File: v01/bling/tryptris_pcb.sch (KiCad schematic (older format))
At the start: 133 parts, among them J1 USB_C_Receptacle_USB2.0, J2 I2C-L, J3 I2C-R, J4 AVR-ISP-6, SW1 Reset, U1 ATmega32U4-AU, U2 MCP23017_SO, U5 PRTR5V0U2X, Y1 16Mhz

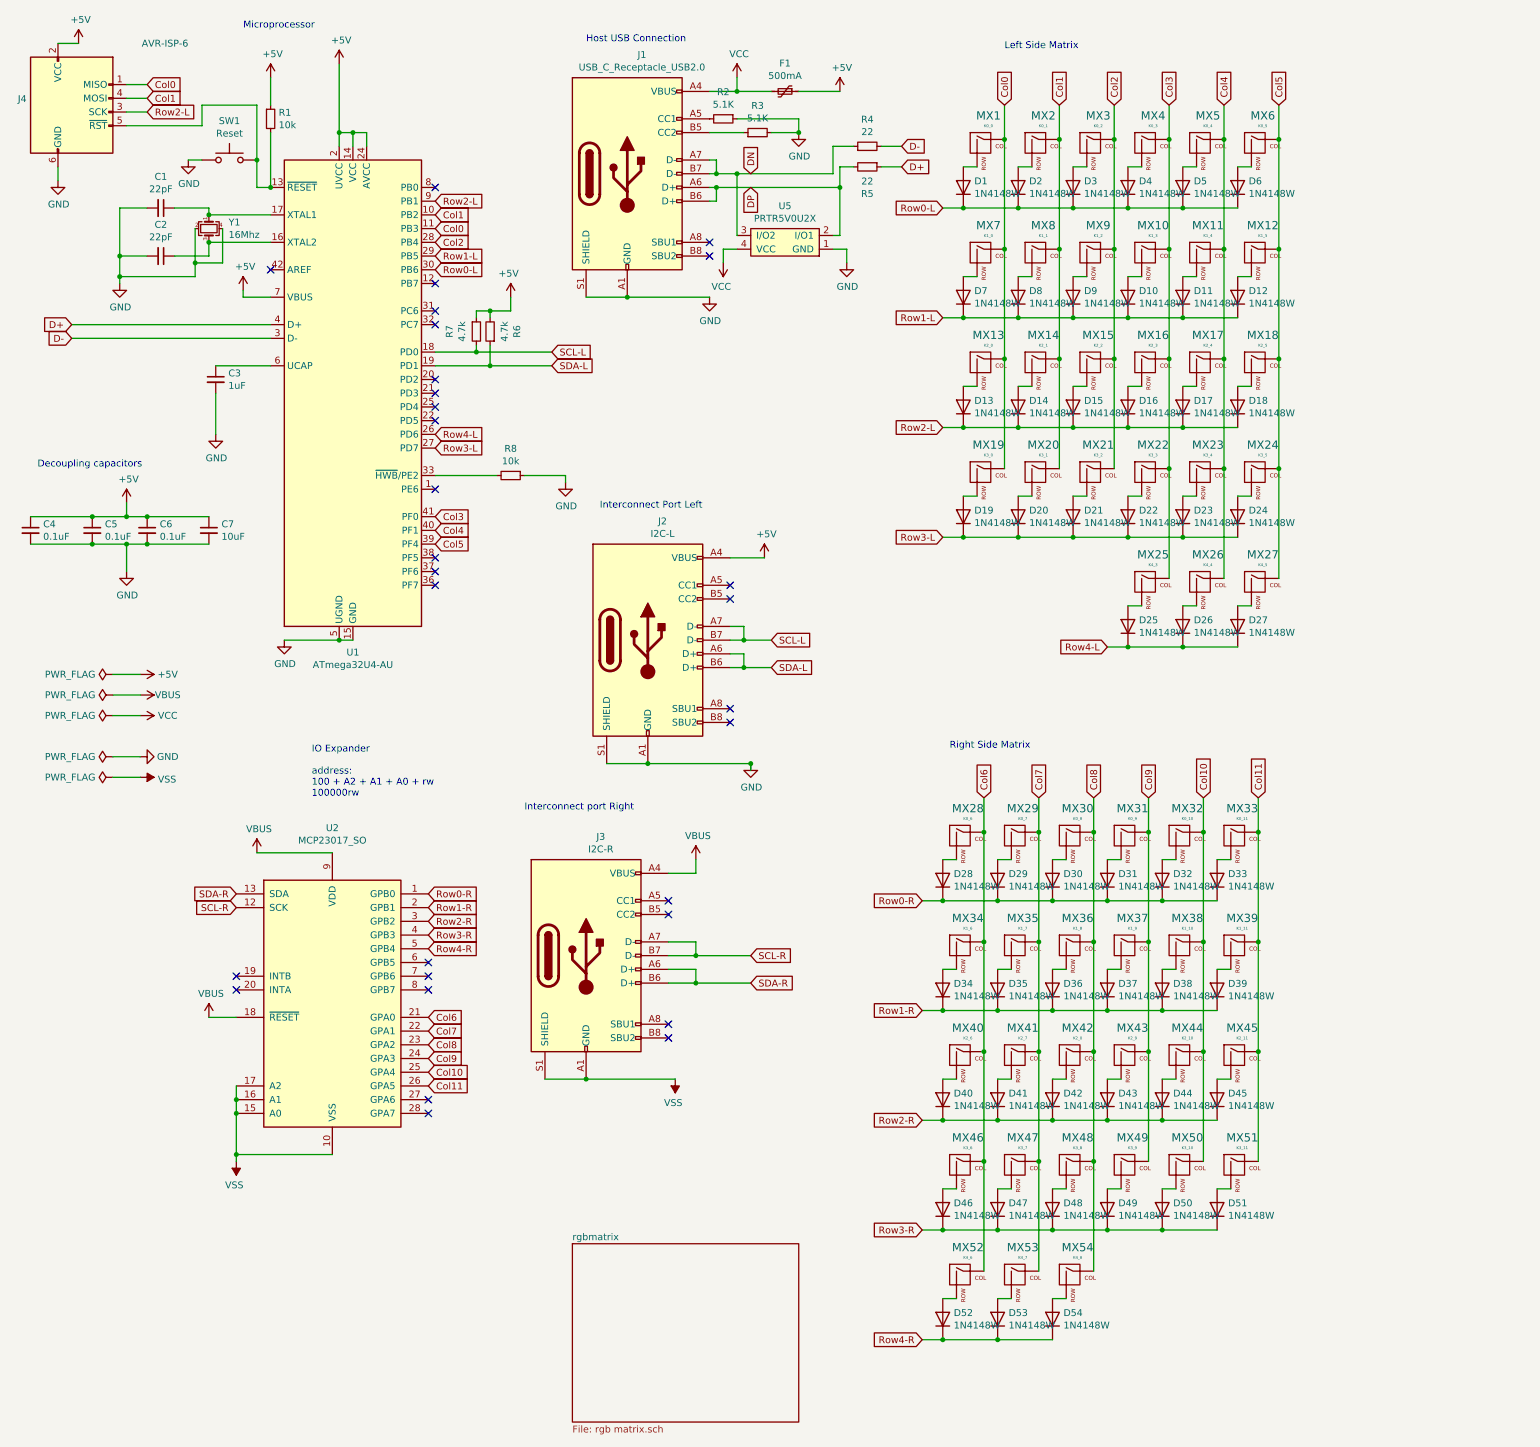
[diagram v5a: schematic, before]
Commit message: Add ESD circuits to bling interconnects.
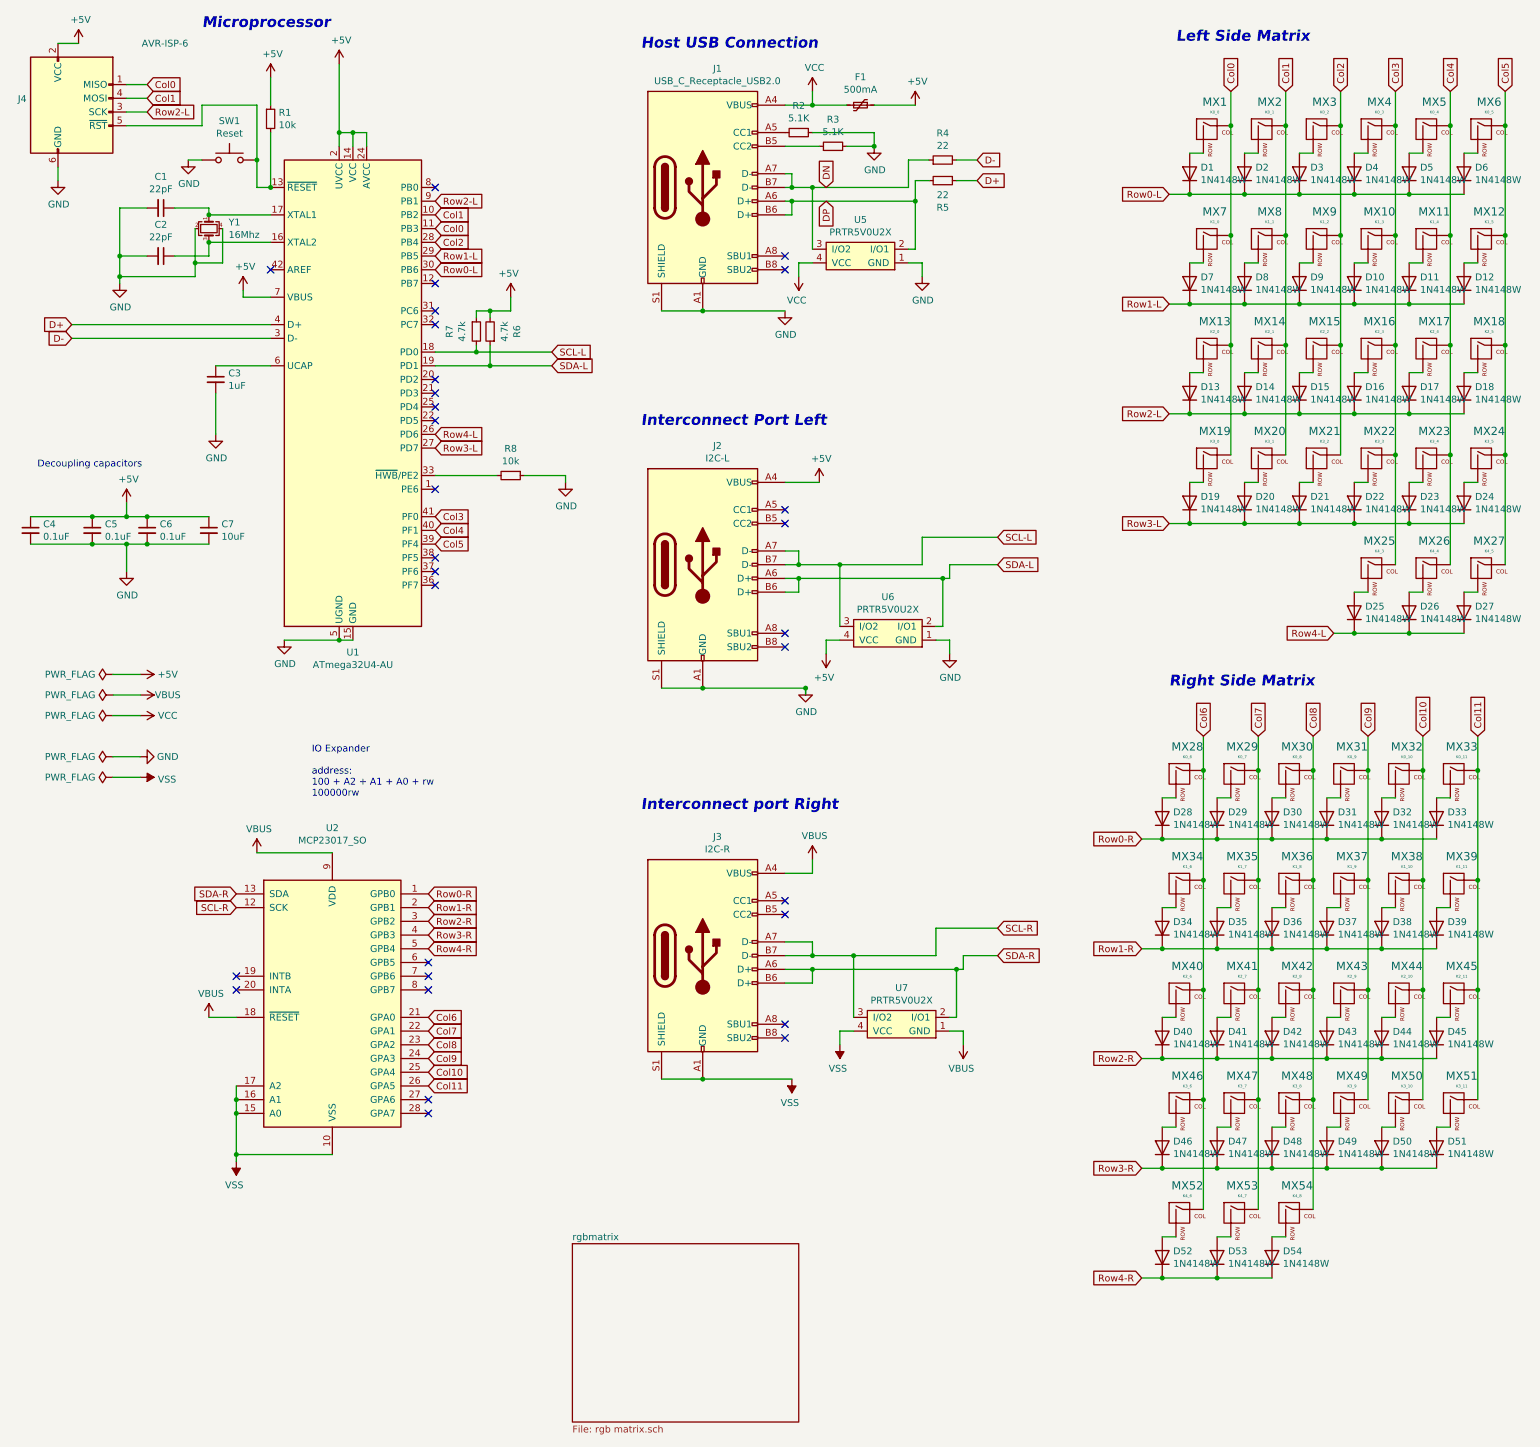
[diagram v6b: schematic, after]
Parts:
- added U6, U7: PRTR5V0U2X, Keebio-Parts:SOT-143B, symbol keebio:PRTR5V0U2X
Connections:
- net +5V: now also U6.4 (VCC)
- net GND: now also U6.1 (GND)
- net SCL-L: now also U6.3 (I/O2)
- net SCL-R: now also U7.3 (I/O2)
- net SDA-L: now also U6.2 (I/O1)
- net SDA-R: now also U7.2 (I/O1)
- net VBUS: now also U7.1 (GND)
- net VSS: now also U7.4 (VCC)
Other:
- moved on the sheet: D1, D10, D11, D12, D13, D14, D15, D16, D17, D18, D19, D2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
